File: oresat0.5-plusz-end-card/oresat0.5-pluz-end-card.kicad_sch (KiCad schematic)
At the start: 38 parts, among them J1 J-SAMTEC-TFM-120-01-L-D-RA, J2 Harwin M55-7101242R, J3 Harwin M55-7101242R, J4 Harwin M55-7101242R, J5 Harwin M55-7101242R, J6 Conn_Coaxial

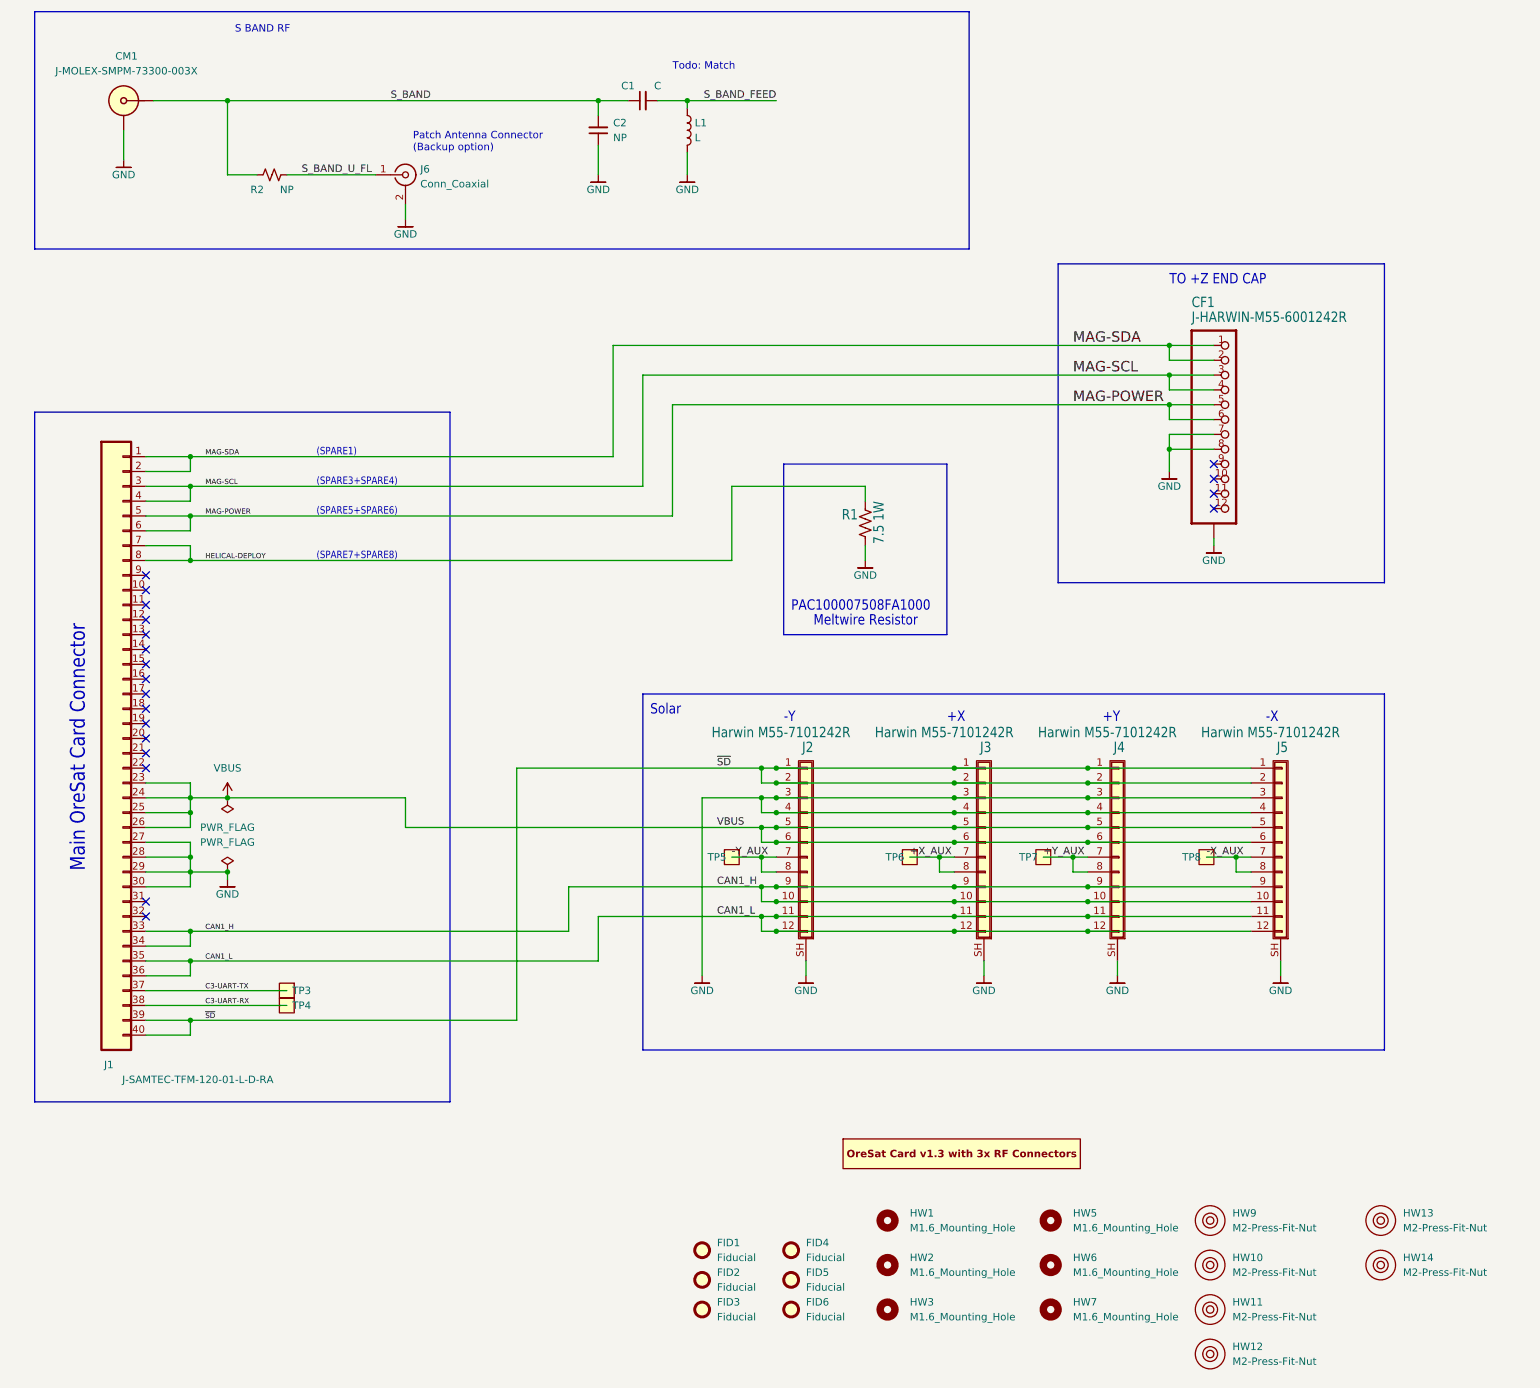
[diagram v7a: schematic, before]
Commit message: Updated date, and unecessary and obsessive widening and smoothing of planes.
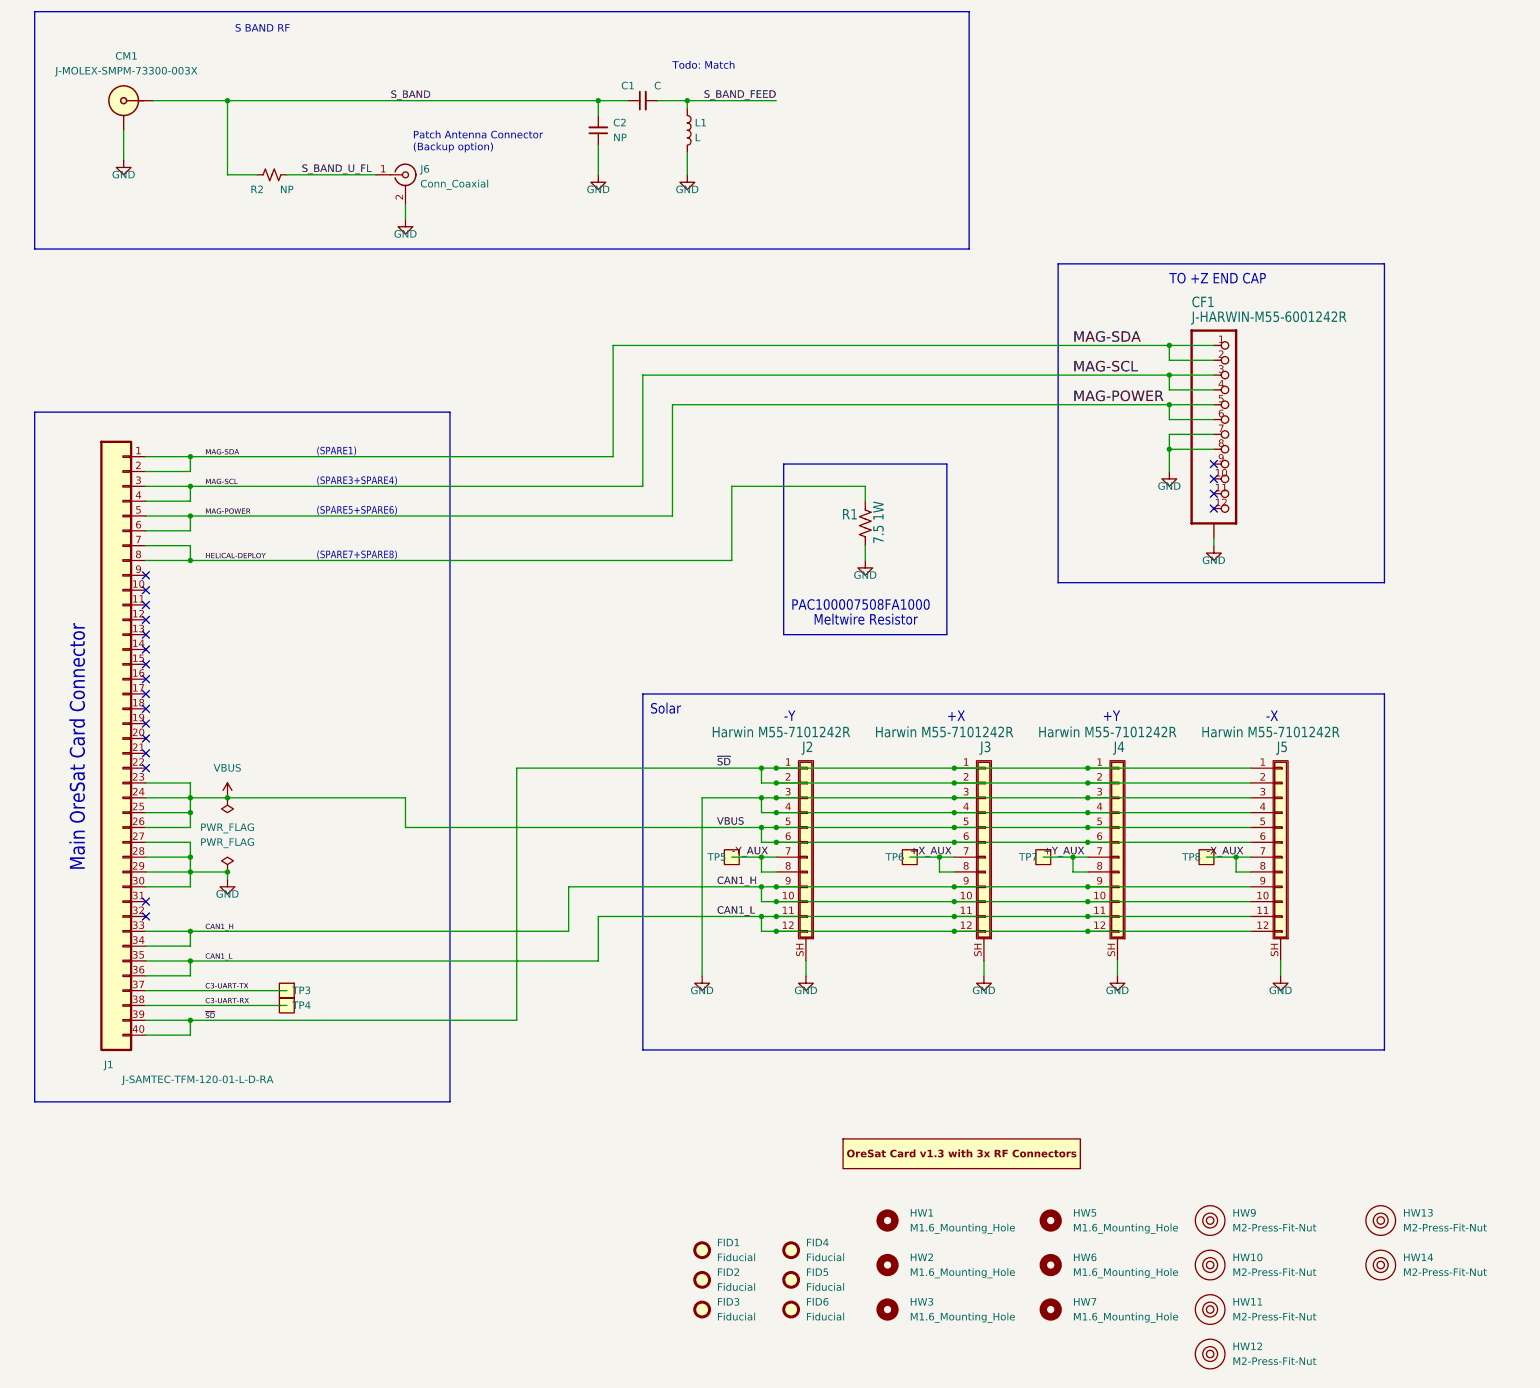
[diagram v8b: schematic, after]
